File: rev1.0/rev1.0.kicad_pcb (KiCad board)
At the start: 2 copper layers, 39.4 x 27.9 mm, 14 parts, among them SW1 SW_DIP_x05, U1 74HC595, U2 74HC595, U3 74HC165

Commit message: More wokr. Må bare koble sammen headers og registere
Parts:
- added J1: Conn_01x06_Pin, Connector_PinHeader_2.54mm:PinHeader_1x06_P2.54mm_Horizontal, F.Cu at (158.8, 89.5)
- added J3: Conn_01x06_Socket, timezoneClock:flatcable conn 6, B.Cu at (149.8, 90.1)
- added J4: Conn_01x06_Socket, timezoneClock:flatcable conn 6, B.Cu at (149.8, 110.6)
- moved U2 21.0 mm to (161.2, 98.4), turned to 0 degrees
- moved U1 12.1 mm to (174.1, 100.3), turned to 180 degrees
- moved RN4 7.31 mm to (158.3, 96.5), turned to 0 degrees
- moved RN5 6.43 mm to (158.3, 101.5), turned to 0 degrees
- moved RN6 4.62 mm to (176.9, 101.5)
- moved DIS1 4.62 mm to (167.7, 98.7)
- moved RN3 4.62 mm to (176.9, 96.5)
- moved JP1 3.18 mm to (146.0, 104.1)
- moved JP2 3.18 mm to (146.0, 106.7)
- moved JP3 3.18 mm to (146.0, 109.2)
- moved RN1 3.18 mm to (154.3, 109.2)
- moved RN2 3.18 mm to (154.3, 105.4)
- moved SW1 3.18 mm to (150.0, 95.2)
- moved U3 3.18 mm to (150.5, 99.1)
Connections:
- RN3 pad 1: unconnected-(RN3-R1.1-Pad1) -> Net-(RN3-R1.1)
- RN3 pad 2: unconnected-(RN3-R2.1-Pad2) -> Net-(RN3-R2.1)
- RN3 pad 3: unconnected-(RN3-R3.1-Pad3) -> Net-(RN3-R3.1)
- RN3 pad 4: unconnected-(RN3-R4.1-Pad4) -> Net-(RN3-R4.1)
- RN4 pad 1: unconnected-(RN4-R1.1-Pad1) -> Net-(RN4-R1.1)
- RN4 pad 2: unconnected-(RN4-R2.1-Pad2) -> Net-(RN4-R2.1)
- RN4 pad 3: unconnected-(RN4-R3.1-Pad3) -> Net-(RN4-R3.1)
- RN4 pad 4: unconnected-(RN4-R4.1-Pad4) -> Net-(RN4-R4.1)
- RN5 pad 1: unconnected-(RN5-R1.1-Pad1) -> Net-(RN5-R1.1)
- RN5 pad 2: unconnected-(RN5-R2.1-Pad2) -> Net-(RN5-R2.1)
- RN5 pad 3: unconnected-(RN5-R3.1-Pad3) -> Net-(RN5-R3.1)
- RN5 pad 4: unconnected-(RN5-R4.1-Pad4) -> Net-(RN5-R4.1)
- RN6 pad 1: unconnected-(RN6-R1.1-Pad1) -> Net-(RN6-R1.1)
- RN6 pad 2: unconnected-(RN6-R2.1-Pad2) -> Net-(RN6-R2.1)
- RN6 pad 3: unconnected-(RN6-R3.1-Pad3) -> Net-(RN6-R3.1)
- RN6 pad 4: unconnected-(RN6-R4.1-Pad4) -> Net-(RN6-R4.1)
- U1 pad 1: unconnected-(U1-QB-Pad1) -> Net-(RN3-R3.1)
- U1 pad 15: unconnected-(U1-QA-Pad15) -> Net-(RN3-R4.1)
- U1 pad 16: unconnected-(U1-VCC-Pad16) -> VCC
- U1 pad 2: unconnected-(U1-QC-Pad2) -> Net-(RN3-R2.1)
- U1 pad 3: unconnected-(U1-QD-Pad3) -> Net-(RN3-R1.1)
- U1 pad 4: unconnected-(U1-QE-Pad4) -> Net-(RN6-R4.1)
- U1 pad 5: unconnected-(U1-QF-Pad5) -> Net-(RN6-R3.1)
- U1 pad 6: unconnected-(U1-QG-Pad6) -> Net-(RN6-R2.1)
- U1 pad 7: Net-(U1-QH) -> Net-(RN6-R1.1)
- U1 pad 8: unconnected-(U1-GND-Pad8) -> GND
- U2 pad 1: unconnected-(U2-QB-Pad1) -> Net-(RN5-R3.1)
- U2 pad 14: Net-(U1-QH) -> Net-(RN6-R1.1)
- U2 pad 15: unconnected-(U2-QA-Pad15) -> Net-(RN5-R4.1)
- U2 pad 16: unconnected-(U2-VCC-Pad16) -> VCC
- U2 pad 2: unconnected-(U2-QC-Pad2) -> Net-(RN5-R2.1)
- U2 pad 3: unconnected-(U2-QD-Pad3) -> Net-(RN5-R1.1)
- U2 pad 4: unconnected-(U2-QE-Pad4) -> Net-(RN4-R4.1)
- U2 pad 5: unconnected-(U2-QF-Pad5) -> Net-(RN4-R3.1)
- U2 pad 6: unconnected-(U2-QG-Pad6) -> Net-(RN4-R2.1)
- U2 pad 7: unconnected-(U2-QH-Pad7) -> Net-(RN4-R1.1)
- U2 pad 8: unconnected-(U2-GND-Pad8) -> GND
- U3 pad 16: unconnected-(U3-VCC-Pad16) -> VCC
- U3 pad 8: unconnected-(U3-GND-Pad8) -> GND
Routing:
- net Net-(RN6-R1.1): track 0.00 -> 21.1 mm, vias 0 -> 1
- net Net-(RN4-R4.2): track 0.00 -> 10.7 mm
- net Net-(RN3-R1.2): track 0.00 -> 10.5 mm
- net Net-(RN5-R1.2): track 0.00 -> 10.5 mm
- net Net-(RN4-R3.2): track 0.00 -> 8.86 mm
- net Net-(RN5-R4.1): track 0.00 -> 8.76 mm, vias 0 -> 1
- net Net-(RN3-R2.2): track 0.00 -> 8.71 mm
- net Net-(RN5-R2.2): track 0.00 -> 8.63 mm
- net Net-(RN3-R4.1): track 0.00 -> 7.59 mm, vias 0 -> 1
- net Net-(RN4-R2.2): track 0.00 -> 5.53 mm
- net Net-(RN3-R3.2): track 0.00 -> 5.38 mm
- net Net-(RN5-R3.2): track 0.00 -> 5.30 mm
- net GND: track 7.08 -> 11.3 mm, vias 0 -> 2
- net Net-(RN4-R1.2): track 0.00 -> 3.77 mm
- net Net-(RN3-R4.2): track 0.00 -> 3.69 mm
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- added copper zone on B.Cu, net GND
- added copper zone on F.Cu, net GND
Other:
- board size 39.4 x 27.9 mm -> 38.1 x 27.9 mm
- board text added: "0"
- board text added: "1"
- board text added: "10K"
- board text added: "150R"

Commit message: oop, forgot the PCB changes
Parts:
- added C1: 100nf, Capacitor_SMD:C_0603_1608Metric, B.Cu at (174.0, 94.1)
- added C2: 100nf, Capacitor_SMD:C_0603_1608Metric, B.Cu at (187.2, 96.5)
- added C3: 100nf, Capacitor_SMD:C_0603_1608Metric, B.Cu at (187.2, 99.1)
- moved J1 23.6 mm to (161.3, 113.0), turned to -90 degrees
- moved J4 20.1 mm to (169.9, 109.8)
- moved J3 20.1 mm to (169.9, 90.7)
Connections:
- J1 pad 1: Data Out -> PISO out
- J1 pad 2: Data In -> SIPO in
- J1 pad 5: 5V -> VCC
- J3 pad 1: Data Out -> PISO in
- J3 pad 2: Data In -> SIPO out
- J3 pad 5: 5V -> VCC
- J4 pad 1: Data Out -> PISO out
- J4 pad 2: Data In -> SIPO in
- J4 pad 5: 5V -> VCC
- RN4 pad 1: Net-(RN4-R1.1) -> SIPO out
- U1 pad 10: unconnected-(U1-~{SRCLR}-Pad10) -> VCC
- U1 pad 11: unconnected-(U1-SRCLK-Pad11) -> Clock
- U1 pad 12: unconnected-(U1-RCLK-Pad12) -> Shift/load
- U1 pad 13: unconnected-(U1-~{OE}-Pad13) -> GND
- U1 pad 14: unconnected-(U1-SER-Pad14) -> SIPO in
- U2 pad 10: unconnected-(U2-~{SRCLR}-Pad10) -> VCC
- U2 pad 11: unconnected-(U2-SRCLK-Pad11) -> Clock
- U2 pad 12: unconnected-(U2-RCLK-Pad12) -> Shift/load
- U2 pad 13: unconnected-(U2-~{OE}-Pad13) -> GND
- U2 pad 7: Net-(RN4-R1.1) -> SIPO out
- U3 pad 1: unconnected-(U3-~{PL}-Pad1) -> Shift/load
- U3 pad 10: unconnected-(U3-DS-Pad10) -> PISO in
- U3 pad 15: unconnected-(U3-~{CE}-Pad15) -> GND
- U3 pad 2: unconnected-(U3-CP-Pad2) -> Clock
- U3 pad 9: unconnected-(U3-Q7-Pad9) -> PISO out
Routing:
- net PISO out: track 0.00 -> 81.2 mm, vias 0 -> 1
- net VCC: track 19.2 -> 59.9 mm
- net Shift/load: track 0.00 -> 34.1 mm
- net PISO in: track 0.00 -> 30.4 mm
- net Clock: track 0.00 -> 28.5 mm
- net SIPO in: track 0.00 -> 16.5 mm
- net GND: track 11.3 -> 13.1 mm
- net SIPO out: track 0.00 -> 1.30 mm, vias 0 -> 1
- net Net-(RN4-R1.1): track 1.30 -> 0.00 mm, vias 1 -> 0
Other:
- board size 38.1 x 27.9 mm -> 38.1 x 30.5 mm

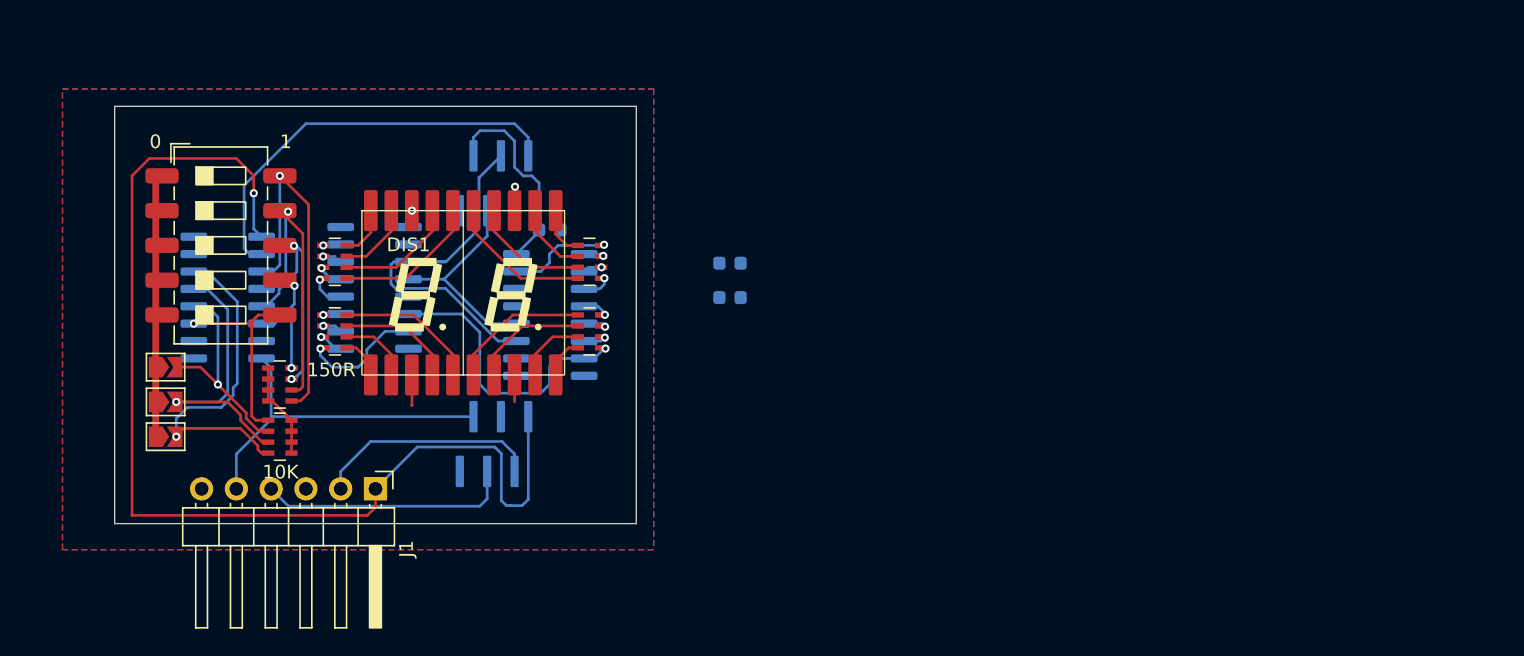
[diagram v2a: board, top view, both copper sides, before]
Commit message: Gikk over til 4-lags for å få det mye mindre.
Byttet også over til en full 8pin DIP-swith, og mindre pakke en jeg hadde først
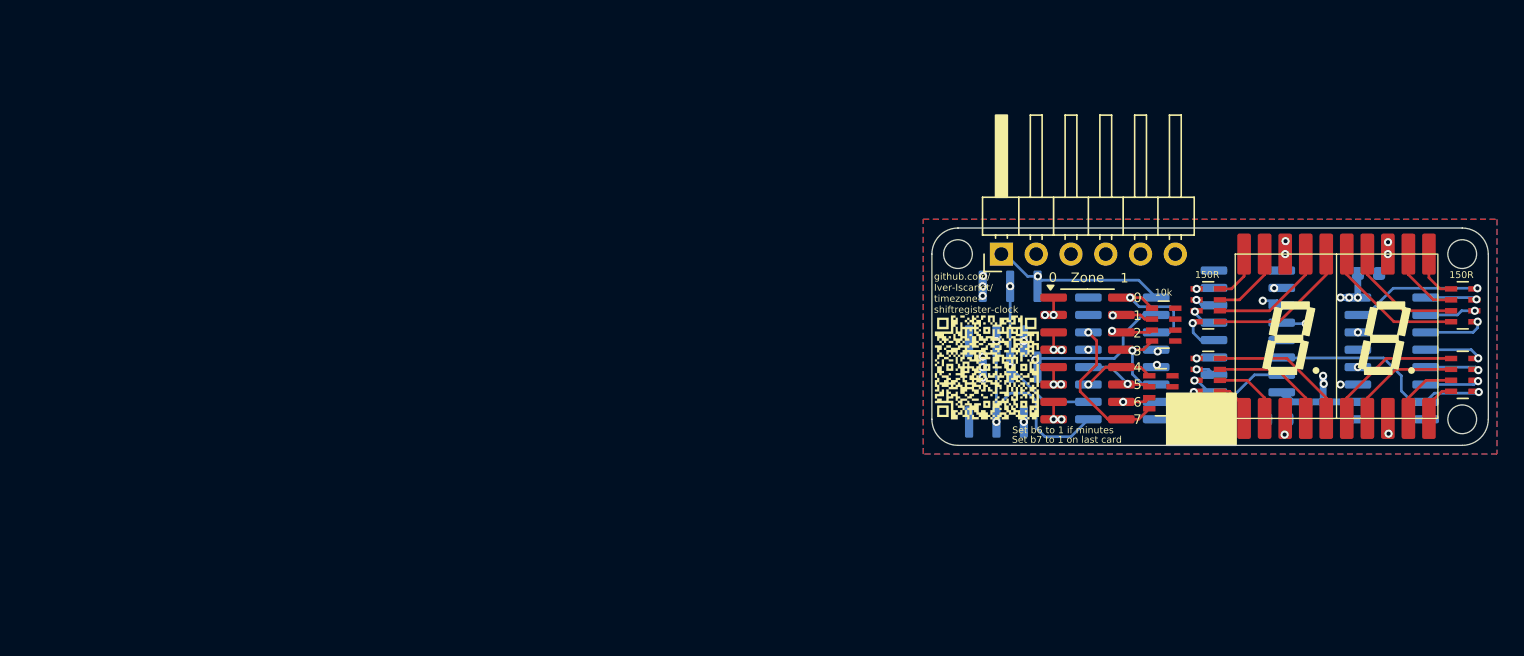
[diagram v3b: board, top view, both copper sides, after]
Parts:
- removed JP1, JP2, JP3: SolderJumper_2_Open, Jumper:SolderJumper-2_P1.3mm_Open_TrianglePad1.0x1.5mm
- removed SW1: SW_DIP_x05, Button_Switch_SMD:SW_DIP_SPSTx05_Slide_6.7x14.26mm_W8.61mm_P2.54mm_LowProfile
- added G***: LOGO, LOGO, F.Cu at (205.9, 104.2)
- added Zone: SW_DIP_x08, Package_SO:SOIC-16_3.9x9.9mm_P1.27mm, F.Cu at (213.3, 103.5)
- moved U3 65.5 mm to (215.8, 103.5)
- moved RN2 64.7 mm to (218.9, 101.0), turned to 180 degrees
- moved RN1 64.4 mm to (218.7, 106.0)
- moved DIS1 63.9 mm to (231.5, 101.9)
- moved RN3 63.9 mm to (240.7, 99.6)
- moved RN6 63.9 mm to (240.7, 104.7)
- moved RN4 63.9 mm to (222.1, 99.6)
- moved RN5 63.9 mm to (222.1, 104.7)
- moved U2 63.9 mm to (225.0, 101.5)
- moved U1 61.5 mm to (235.5, 103.5)
- moved C1 59.9 mm to (233.8, 97.3)
- moved J1 48.8 mm to (207.0, 95.9), turned to 90 degrees
- moved C2 41.5 mm to (227.1, 108.0), turned to 0 degrees
- moved J3 40.3 mm to (207.1, 106.1)
- moved J4 38.4 mm to (207.1, 100.2)
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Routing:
- net PISO out: track 81.2 -> 13.4 mm
- net VCC: track 59.9 -> 21.0 mm, vias 0 -> 23
- net SIPO out: track 1.30 -> 23.5 mm, vias 1 -> 2
- net Shift/load: track 34.1 -> 55.1 mm, vias 0 -> 4
- net PISO in: track 30.4 -> 10.8 mm, vias 0 -> 1
- net Net-(RN2-R4.2): track 26.9 -> 8.83 mm
- net Clock: track 28.5 -> 46.5 mm, vias 0 -> 4
- net SIPO in: track 16.5 -> 31.4 mm, vias 0 -> 2
- net Net-(RN2-R3.2): track 21.4 -> 6.73 mm, vias 1 -> 2
- net Net-(RN1-R2.2): track 21.5 -> 7.03 mm, vias 1 -> 2
- net Net-(RN1-R1.2): track 25.2 -> 11.3 mm
- net GND: track 13.1 -> 0.00 mm, vias 2 -> 6
- net Net-(RN2-R2.2): track 17.7 -> 6.68 mm
- net Net-(RN1-R3.2): track 16.0 -> 5.48 mm
- net Net-(RN1-R4.2): track 15.5 -> 5.23 mm
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- added copper zone on In1.Cu, net VCC
- added copper zone on In2.Cu, net VCC
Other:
- board size 38.1 x 30.5 mm -> 40.6 x 15.9 mm
- copper layers 2 -> 4
- board text added: "10k"
- board text added: "2"
- board text added: "3"
- board text added: "4"
- board text added: "5"
- board text added: "6"
- board text added: "7"
- board text added: "74HC165"
- board text added: "74HC595"
- board text added: "Set b6 to 1 if minutes"
- board text added: "Set b7 to 1 on last card"
- board text added: "github.com/ Iver-Iscariot/ timezone- shiftregister-clock"
- board text removed: "10K"

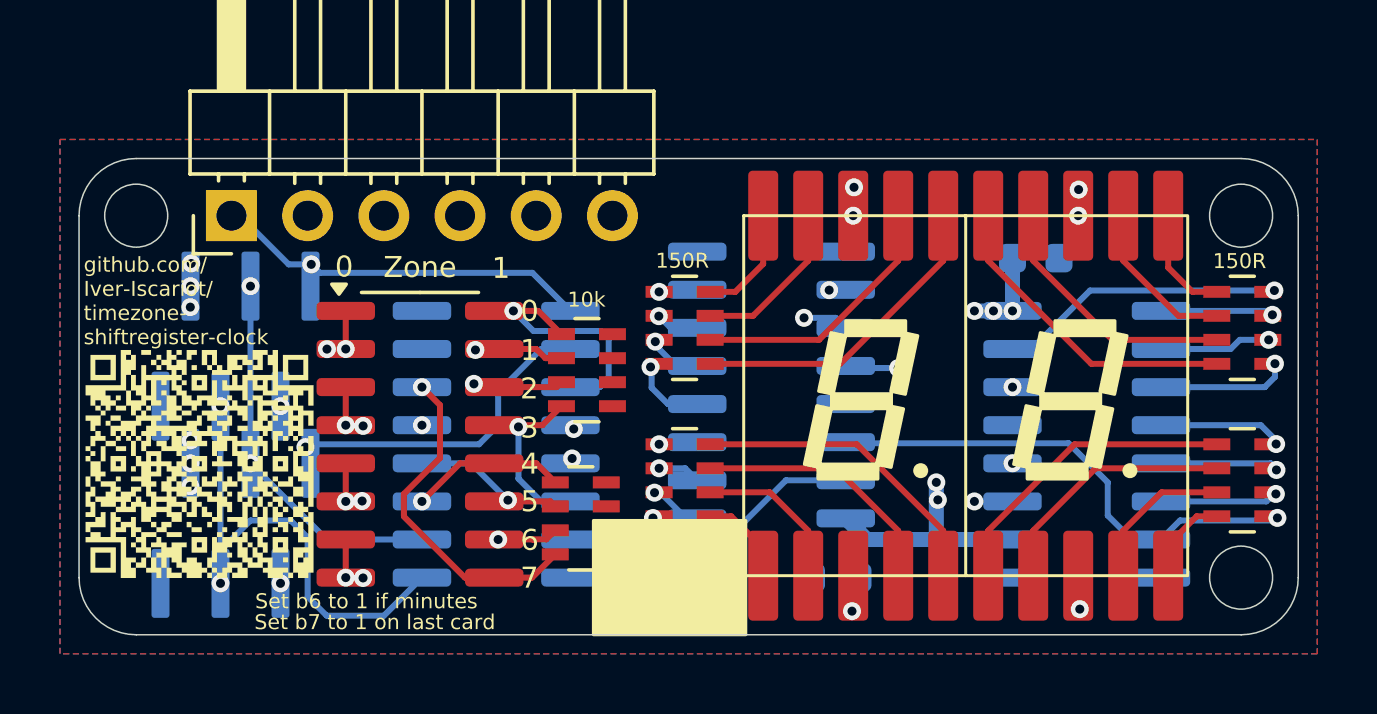
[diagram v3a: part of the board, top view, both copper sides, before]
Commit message: Completed pcb for module, and started an arduino socket w/ interconnect
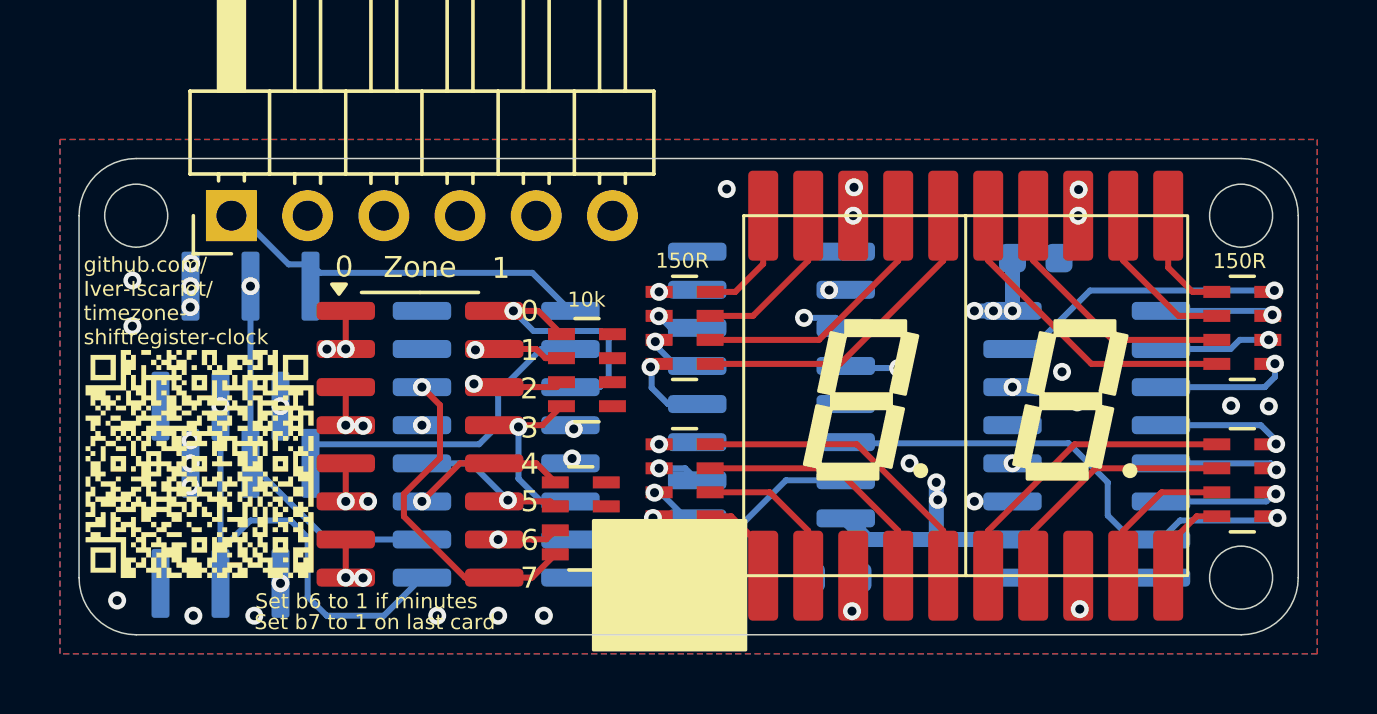
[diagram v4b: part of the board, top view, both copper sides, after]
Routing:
- net VCC: vias 23 -> 29
- net Shift/load: vias 4 -> 3
- net PISO out: vias 1 -> 0
- net PISO in: vias 1 -> 0
- net GND: vias 6 -> 16
- net Clock: vias 4 -> 3
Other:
- board text added: "By Iver Iscariot Søbakk"
- board text added: "TimeZone clock REV 1.0"
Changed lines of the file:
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@@
 	(gr_rect
 		(start 219.075 106.045)
-		(end 224.155 109.855)
+		(end 224.155 110.363)
 		(stroke
 			(width 0.1)
@@
 		)
 	)
+	(gr_text "By Iver Iscariot Søbakk"
+		(at 238.759999 96.384228 0)
+		(layer "B.SilkS")
+		(effects
+			(font
+				(size 0.6 0.6)
+				(thickness 0.1)
+			)
+			(justify left bottom mirror)
+		)
+	)
+	(gr_text "TimeZone clock REV 1.0\n"
+		(at 238.995999 95.368228 0)
+		(layer "B.SilkS")
+		(effects
+			(font
+				(size 1 1)
+				(thickness 0.1)
+			)
+			(justify left bottom mirror)
+		)
+	)
 	(gr_text "74HC165"
 		(at 218.428864 98.185959 0)
@@
 	)
 	(segment
+		(start 210.82 100.33)
+		(end 210.82 99.06)
+		(width 0.2)
+		(layer "F.Cu")
+		(net 1)
+	)
+	(segment
+		(start 210.82 107.95)
+		(end 210.82 106.68)
+		(width 0.2)
+		(layer "F.Cu")
+		(net 1)
+	)
+	(segment
+		(start 210.82 102.87)
+		(end 210.82 101.6)
+		(width 0.2)
+		(layer "F.Cu")
+		(net 1)
+	)
+	(segment
 		(start 210.82 105.41)
 		(end 210.82 104.14)
@@
 		(net 1)
 	)
-	(segment
-		(start 210.82 100.33)
-		(end 210.82 99.06)
-		(width 0.2)
-		(layer "F.Cu")
-		(net 1)
-	)
-	(segment
-		(start 210.82 107.95)
-		(end 210.82 106.68)
-		(width 0.2)
-		(layer "F.Cu")
-		(net 1)
-	)
-	(segment
-		(start 210.82 102.87)
-		(end 210.82 101.6)
-		(width 0.2)
-		(layer "F.Cu")
+	(via
+		(at 203.2 108.712)
+		(size 0.6)
+		(drill 0.3)
+		(layers "F.Cu" "B.Cu")
+		(free yes)
 		(net 1)
 	)
@@
 	)
 	(via
+		(at 241.589833 102.239631)
+		(size 0.6)
+		(drill 0.3)
+		(layers "F.Cu" "B.Cu")
+		(free yes)
+		(net 1)
+	)
+	(via
 		(at 210.82 107.95)
 		(size 0.6)
@@
 	)
 	(via
+		(at 223.52 94.996)
+		(size 0.6)
+		(drill 0.3)
+		(layers "F.Cu" "B.Cu")
+		(free yes)
+		(net 1)
+	)
+	(via
 		(at 220.98 107.95)
 		(size 0.6)
@@
 	)
 	(via
+		(at 217.424 109.22)
+		(size 0.6)
+		(drill 0.3)
+		(layers "F.Cu" "B.Cu")
+		(free yes)
+		(net 1)
+	)
+	(via
 		(at 205.645 98.235)
 		(size 0.6)
@@
 	)
 	(via
+		(at 213.868 109.22)
+		(size 0.6)
+		(drill 0.3)
+		(layers "F.Cu" "B.Cu")
+		(free yes)
+		(net 1)
+	)
+	(via
 		(at 211.399255 102.893222)
 		(size 0.6)
@@
 	)
 	(via
-		(at 211.365578 105.396528)
+		(at 211.563851 105.410046)
 		(size 0.6)
 		(drill 0.3)
@@
 		(drill 0.3)
 		(layers "F.Cu" "B.Cu")
+		(net 1)
+	)
+	(via
+		(at 203.708 99.568)
+		(size 0.6)
+		(drill 0.3)
+		(layers "F.Cu" "B.Cu")
+		(free yes)
 		(net 1)
 	)
@@
 	)
 	(via
+		(at 203.708 98.044)
+		(size 0.6)
+		(drill 0.3)
+		(layers "F.Cu" "B.Cu")
+		(free yes)
+		(net 2)
+	)
+	(via
+		(at 235.204 102.108)
+		(size 0.6)
+		(drill 0.3)
+		(layers "F.Cu" "B.Cu")
+		(free yes)
+		(net 2)
+	)
+	(via
 		(at 227.735 95.885)
 		(size 0.6)
@@
 	)
 	(via
+		(at 229.616 104.14)
+		(size 0.6)
+		(drill 0.3)
+		(layers "F.Cu" "B.Cu")
+		(free yes)
+		(net 2)
+	)
+	(via
+		(at 207.772 109.22)
+		(size 0.6)
+		(drill 0.3)
+		(layers "F.Cu" "B.Cu")
+		(free yes)
+		(net 2)
+	)
+	(via
 		(at 227.695226 109.068412)
 		(size 0.6)
@@
 		(drill 0.3)
 		(layers "F.Cu" "B.Cu")
+		(net 2)
+	)
+	(via
+		(at 234.696 101.092)
+		(size 0.6)
+		(drill 0.3)
+		(layers "F.Cu" "B.Cu")
+		(free yes)
+		(net 2)
+	)
+	(via
+		(at 223.52 109.22)
+		(size 0.6)
+		(drill 0.3)
+		(layers "F.Cu" "B.Cu")
+		(free yes)
+		(net 2)
+	)
+	(via
+		(at 222.504 109.22)
+		(size 0.6)
+		(drill 0.3)
+		(layers "F.Cu" "B.Cu")
+		(free yes)
+		(net 2)
+	)
+	(via
+		(at 215.9 109.22)
+		(size 0.6)
+		(drill 0.3)
+		(layers "F.Cu" "B.Cu")
+		(free yes)
+		(net 2)
+	)
+	(via
+		(at 205.74 109.22)
+		(size 0.6)
+		(drill 0.3)
+		(layers "F.Cu" "B.Cu")
+		(free yes)
+		(net 2)
+	)
+	(via
+		(at 240.330558 102.219643)
+		(size 0.6)
+		(drill 0.3)
+		(layers "F.Cu" "B.Cu")
+		(free yes)
 		(net 2)
 	)
@@
 		(net 8)
 	)
-	(via
-		(at 209.670183 97.508615)
-		(size 0.6)
-		(drill 0.3)
-		(layers "F.Cu" "B.Cu")
-		(net 9)
-	)
 	(segment
 		(start 209.670183 97.508615)
@@
 		(net 9)
 	)
-	(via
-		(at 209.475733 103.598945)
-		(size 0.6)
-		(drill 0.3)
-		(layers "F.Cu" "B.Cu")
-		(net 10)
-	)
 	(segment
 		(start 217.335001 100.33)
@@
 	)
 	(via
-		(at 207.645 104.14)
-		(size 0.6)
-		(drill 0.3)
-		(layers "F.Cu" "B.Cu")
-		(net 46)
-	)
-	(via
 		(at 231.775 105.41)
 		(size 0.6)
@@
 		(size 0.6)
 		(drill 0.3)
-		(layers "F.Cu" "B.Cu")
-		(net 47)
-	)
-	(via
-		(at 206.645 108.14)
-		(size 0.6)
-		(drill 0.3)
